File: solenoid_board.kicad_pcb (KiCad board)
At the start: 2 copper layers, 180 x 120 mm, 30 parts, among them J2 MCU_LEFT_LEGS, J3 MCU_RIGHT_LEGS

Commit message: Changed Geometry of PCB, removed edges, cleaned up displays. Next steps: routing.
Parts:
- 7Seg_1, 7Seg_2, 7Seg_3, 7Seg_4, 7Seg_5, 7Seg_6, 7Seg_7, 7Seg_8, 7Seg_9: moved to B.Cu
- moved R330 181.3 mm to (242.8, 50.7)
- moved R336 181.3 mm to (314.8, 50.7)
- moved R337 181.3 mm to (326.8, 50.7)
- moved R338 181.3 mm to (338.8, 50.7)
- moved R331 181.3 mm to (254.8, 50.7)
- moved R332 181.3 mm to (266.8, 50.7)
- moved R333 181.3 mm to (278.8, 50.7)
- moved R334 181.3 mm to (290.8, 50.7)
- moved R335 181.3 mm to (302.8, 50.7)
- moved 7Seg_6 59.5 mm to (161.8, 124.5), turned to 90 degrees
- moved 7Seg_5 55.2 mm to (146.8, 124.5), turned to 90 degrees
- moved 7Seg_4 55.0 mm to (131.8, 124.5), turned to 90 degrees
- moved 7Seg_3 45.6 mm to (116.8, 124.5), turned to 90 degrees
- moved 7Seg_7 43.5 mm to (88.1, 68.7), turned to 90 degrees
- moved 7Seg_1 42.8 mm to (86.8, 124.5), turned to 90 degrees
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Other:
- board outline removed

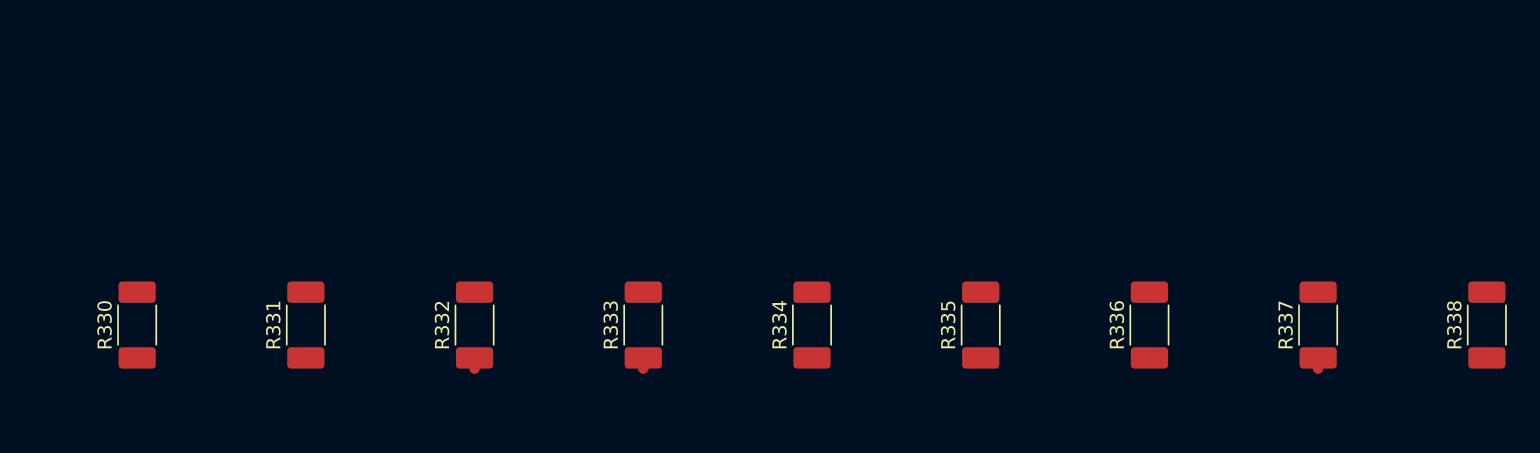
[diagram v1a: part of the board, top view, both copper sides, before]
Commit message: Changed resistor footprints, changed resistor supplier. Still need to route wires.
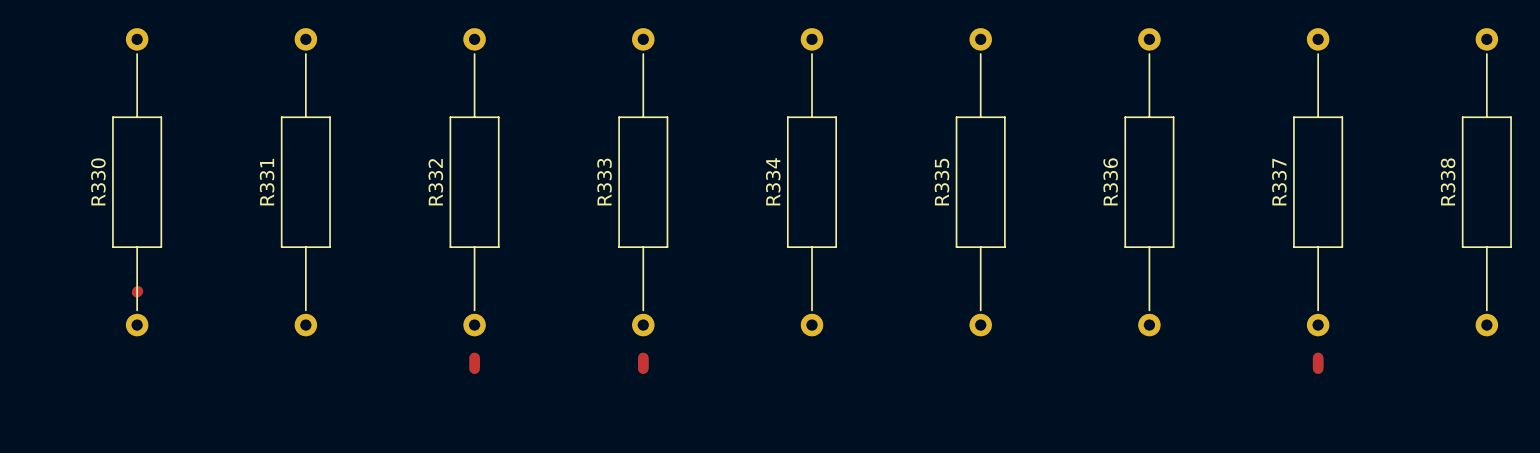
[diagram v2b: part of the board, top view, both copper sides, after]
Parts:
- R330, R331, R332, R333, R334, R335, R336, R337, R338: footprint Resistor_SMD:R_2010_5025Metric_Pad1.52x2.65mm_HandSolder -> Resistor_THT:R_Axial_DIN0309_L9.0mm_D3.2mm_P20.32mm_Horizontal

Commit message: Worked on Geometry of board. Needs to be finalized.
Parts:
- moved R336 232.4 mm to (83.0, 34.8), turned to 0 degrees
- moved R337 228.9 mm to (98.2, 38.9), turned to 0 degrees
- moved R338 225.7 mm to (113.2, 43.2), turned to 0 degrees
- moved R330 163.8 mm to (81.8, 80.9), turned to 0 degrees
- moved R331 161.7 mm to (96.8, 85.3), turned to 0 degrees
- moved R332 159.9 mm to (111.7, 89.7), turned to 0 degrees
- moved R333 158.1 mm to (126.6, 93.7), turned to 0 degrees
- moved R334 156.3 mm to (141.8, 97.7), turned to 0 degrees
- moved R335 154.8 mm to (156.8, 102.0), turned to 0 degrees
- moved C0.1nF0 21.6 mm to (215.8, 107.8)
- moved Prt_IC1 21.6 mm to (200.8, 104.7)
- moved J2 21.6 mm to (196.6, 60.3)
- moved CP0 21.6 mm to (220.6, 72.9)
- moved GND1 21.6 mm to (222.4, 113.0)
- moved J3 21.6 mm to (217.0, 70.4)
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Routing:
- net /First_Display: track 0.00 -> 43.6 mm
- net /Second_Display: track 0.00 -> 39.3 mm
- net /Third_Display: track 0.76 -> 34.9 mm
- net /Seventh_Display: track 0.00 -> 34.0 mm
- net /Fourth_Display: track 0.76 -> 30.9 mm
- net /Eigth_Display: track 0.76 -> 30.6 mm
- net /Fifth_Display: track 0.00 -> 26.8 mm
- net /Ninth_Display: track 0.00 -> 25.6 mm
- net /Sixth_Display: track 0.00 -> 22.6 mm
- net /DP: track 1.20 -> 0.00 mm

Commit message: Rearranged Component Geometry, switched out Transciever Resistor footprints, Routed Some wires.
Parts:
- R10, R11: footprint Resistor_SMD:R_2010_5025Metric_Pad1.52x2.65mm_HandSolder -> Resistor_THT:R_Axial_DIN0309_L9.0mm_D3.2mm_P20.32mm_Horizontal
- moved 7Seg_1 82.3 mm to (127.8, 53.2)
- moved 7Seg_2 82.3 mm to (142.8, 53.2)
- moved 7Seg_3 82.3 mm to (157.8, 53.2)
- moved R330 73.8 mm to (122.9, 19.6)
- moved R331 73.1 mm to (137.8, 24.8)
- moved R332 72.5 mm to (152.9, 30.0)
- moved R333 59.0 mm to (77.2, 61.5)
- moved R334 58.9 mm to (92.1, 66.0)
- moved R335 58.8 mm to (107.1, 70.4)
- moved R338 56.3 mm to (152.5, 83.6)
- moved 7Seg_7 56.2 mm to (127.6, 108.7)
- moved 7Seg_8 56.2 mm to (142.6, 108.7)
- moved 7Seg_9 56.2 mm to (157.6, 108.7)
- moved R336 56.2 mm to (122.5, 74.8)
- moved R337 56.2 mm to (137.7, 78.9)
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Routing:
- net /D10: track 0.00 -> 148.2 mm
- net /D13: track 0.00 -> 136.3 mm
- net /D9: track 0.00 -> 131.0 mm
- net /D12: track 0.00 -> 118.1 mm
- net /D6: track 0.00 -> 113.5 mm
- net /D11: track 0.00 -> 100.6 mm
- net /A3: track 0.00 -> 96.1 mm
- net /D5: track 0.00 -> 95.3 mm
- net /SCL: track 0.00 -> 77.2 mm
- net /SDA: track 0.00 -> 59.4 mm
- net /Fourth_Display: track 30.9 -> 47.1 mm
- net /Fifth_Display: track 26.8 -> 42.7 mm
- net /Sixth_Display: track 22.6 -> 38.3 mm
- net /RJ45_5: track 73.8 -> 61.8 mm, vias 0 -> 1
- net /Third_Display: track 34.9 -> 23.3 mm
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
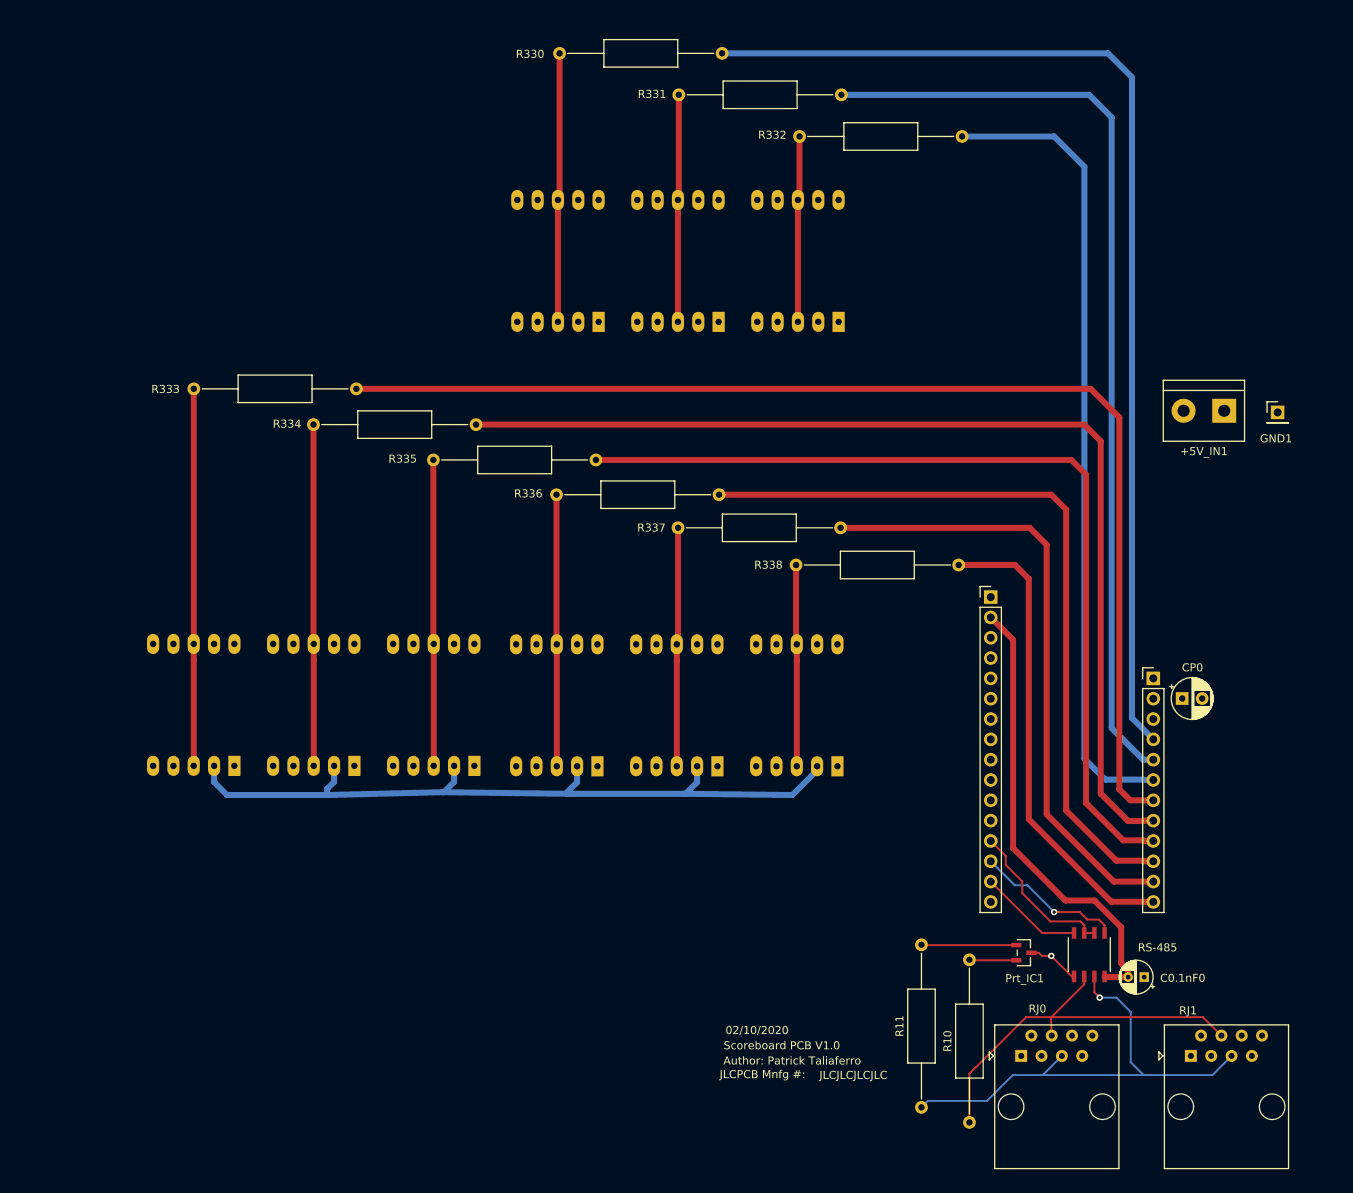
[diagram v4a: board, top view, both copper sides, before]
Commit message: Finished Routing and generated new .gbr files. I am unsatisfied with the size of the board, and the geometry may need to be moved around to allow ball count to be displayed underneath the score.
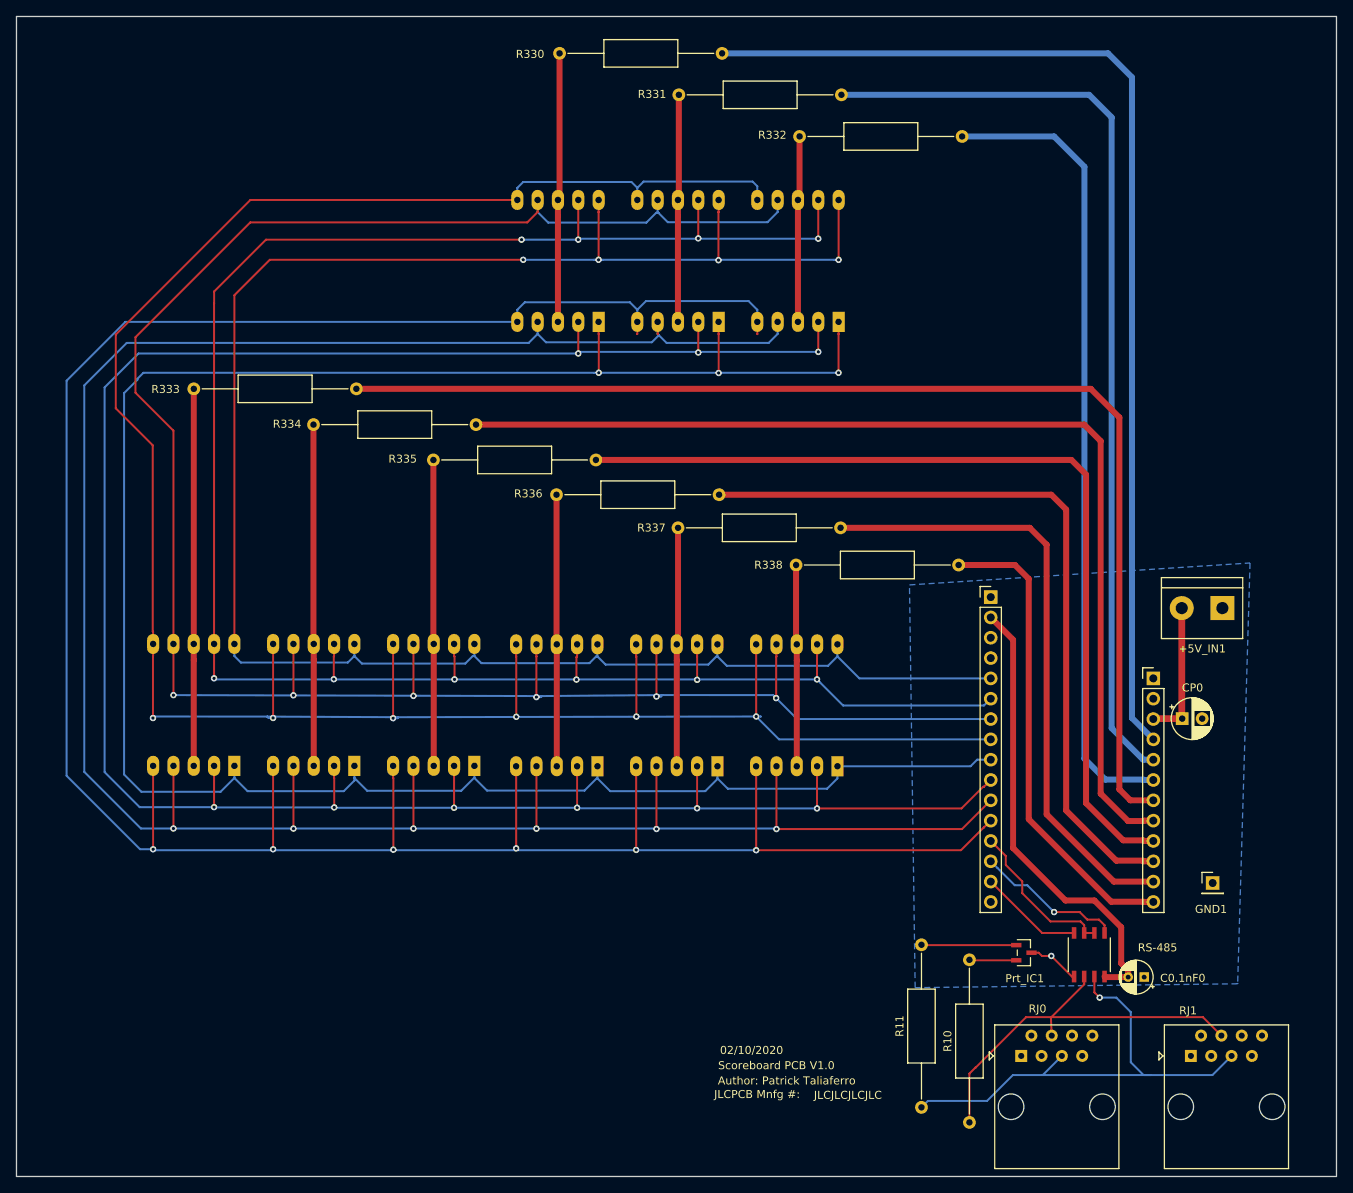
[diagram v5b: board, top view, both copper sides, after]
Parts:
- moved GND1 59.4 mm to (204.5, 123.3)
- moved +5V_IN1 24.7 mm to (205.7, 89.0)
- moved CP0 2.51 mm to (200.7, 102.8)
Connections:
- 7Seg_1 pad 10: /G -> /A0
- 7Seg_1 pad 2: /A3 -> /A5
- 7Seg_1 pad 4: /A2 -> /C
- 7Seg_1 pad 6: /A1 -> /A3
- 7Seg_1 pad 9: /A5 -> /A1
- 7Seg_2 pad 10: /G -> /A0
- 7Seg_2 pad 2: /A3 -> /A5
- 7Seg_2 pad 4: /A2 -> /C
- 7Seg_2 pad 6: /A1 -> /A3
- 7Seg_2 pad 9: /A5 -> /A1
- 7Seg_3 pad 10: /G -> /A0
- 7Seg_3 pad 2: /A3 -> /A5
- 7Seg_3 pad 4: /A2 -> /C
- 7Seg_3 pad 6: /A1 -> /A3
- 7Seg_3 pad 9: /A5 -> /A1
- 7Seg_4 pad 10: /G -> /A0
- 7Seg_4 pad 2: /A3 -> /A5
- 7Seg_4 pad 4: /A2 -> /C
- 7Seg_4 pad 6: /A1 -> /A3
- 7Seg_4 pad 9: /A5 -> /A1
- 7Seg_5 pad 10: /G -> /A0
- 7Seg_5 pad 2: /A3 -> /A5
- 7Seg_5 pad 4: /A2 -> /C
- 7Seg_5 pad 6: /A1 -> /A3
- 7Seg_5 pad 9: /A5 -> /A1
- 7Seg_6 pad 10: /G -> /A0
- 7Seg_6 pad 2: /A3 -> /A5
- 7Seg_6 pad 4: /A2 -> /C
- 7Seg_6 pad 6: /A1 -> /A3
- 7Seg_6 pad 9: /A5 -> /A1
- 7Seg_7 pad 10: /G -> /A0
- 7Seg_7 pad 2: /A3 -> /A5
- 7Seg_7 pad 4: /A2 -> /C
- 7Seg_7 pad 6: /A1 -> /A3
- 7Seg_7 pad 9: /A5 -> /A1
- 7Seg_8 pad 10: /G -> /A0
- 7Seg_8 pad 2: /A3 -> /A5
- 7Seg_8 pad 4: /A2 -> /C
- 7Seg_8 pad 6: /A1 -> /A3
- 7Seg_8 pad 9: /A5 -> /A1
- 7Seg_9 pad 10: /G -> /A0
- 7Seg_9 pad 2: /A3 -> /A5
- 7Seg_9 pad 4: /A2 -> /C
- 7Seg_9 pad 6: /A1 -> /A3
- 7Seg_9 pad 9: /A5 -> /A1
- J2 pad 11: /G -> /C
- J2 pad 5: /A -> /A0
- J2 pad 7: /A2 -> /A
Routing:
- net /DP: track 0.00 -> 331.7 mm, vias 0 -> 6
- net /C: track 0.00 -> 310.4 mm, vias 0 -> 6
- net /A5: track 0.00 -> 296.1 mm, vias 0 -> 9
- net /A4: track 0.00 -> 283.2 mm, vias 0 -> 3
- net /A: track 0.00 -> 279.7 mm, vias 0 -> 6
- net /A1: track 0.00 -> 262.2 mm, vias 0 -> 10
- net /A0: track 0.00 -> 252.2 mm, vias 0 -> 4
- net /A3: track 96.1 -> 296.7 mm, vias 0 -> 6
- net +5V: track 0.00 -> 17.5 mm
- added copper zone on B.Cu, net GND
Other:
- board outline added: 165 x 145 mm

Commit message: Added Mounting Holes
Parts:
- added REF**: MountingHole_2.7mm_M2.5, MountingHole:MountingHole_2.7mm_M2.5, F.Cu at (60.0, 155.0)
- added REF**: MountingHole_2.7mm_M2.5, MountingHole:MountingHole_2.7mm_M2.5, F.Cu at (60.0, 20.0)
- added REF**: MountingHole_2.7mm_M2.5, MountingHole:MountingHole_2.7mm_M2.5, F.Cu at (220.0, 155.0)
- added REF**: MountingHole_2.7mm_M2.5, MountingHole:MountingHole_2.7mm_M2.5, F.Cu at (220.0, 20.0)
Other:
- board size 165 x 145 mm -> 170 x 145 mm

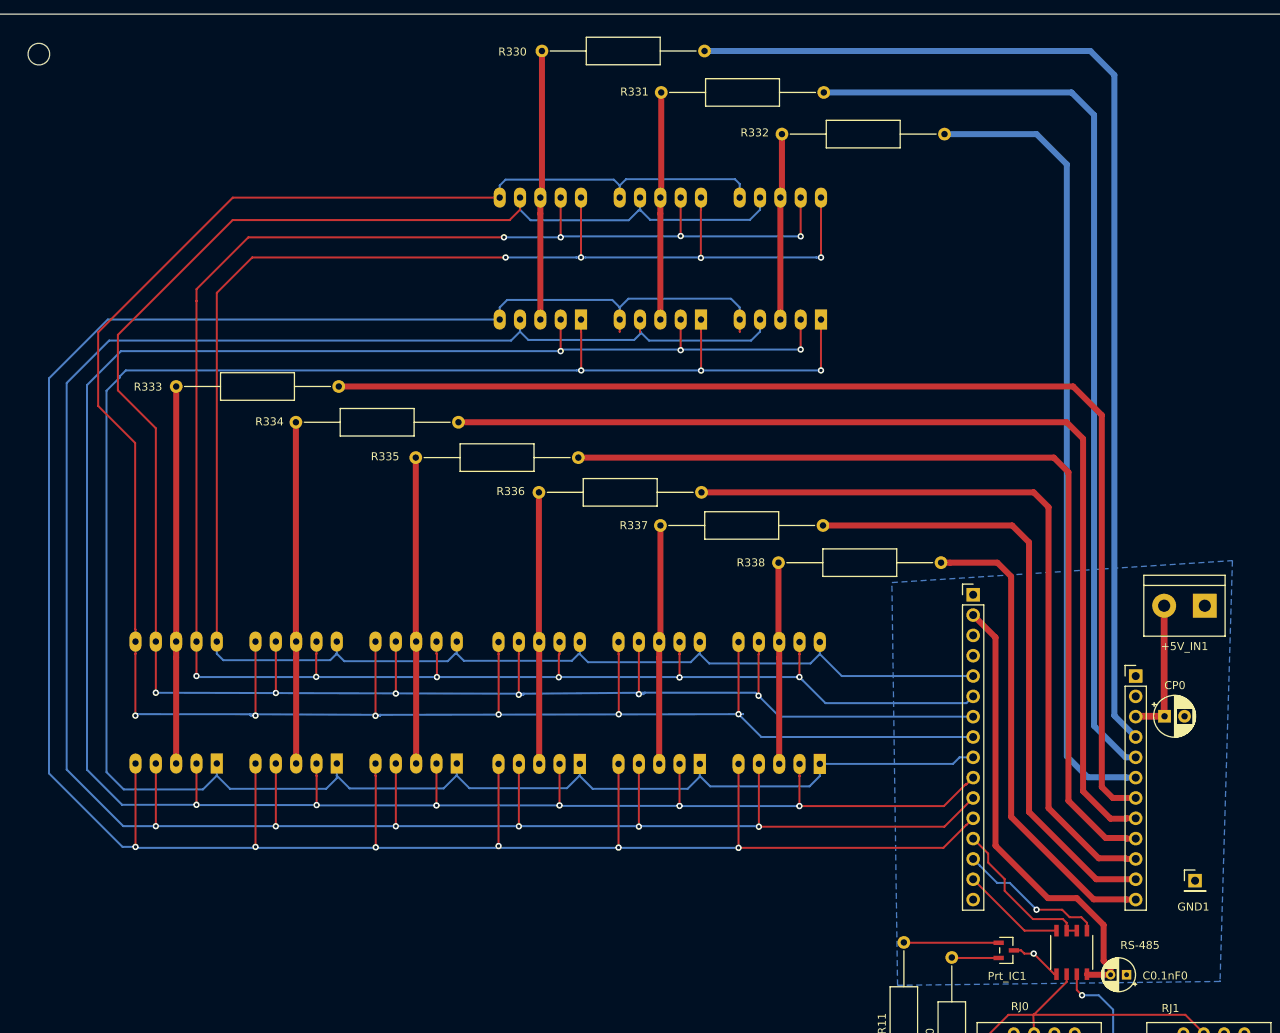
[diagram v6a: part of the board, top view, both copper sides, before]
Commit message: Deleted all the wire routes related to the scoreboard.
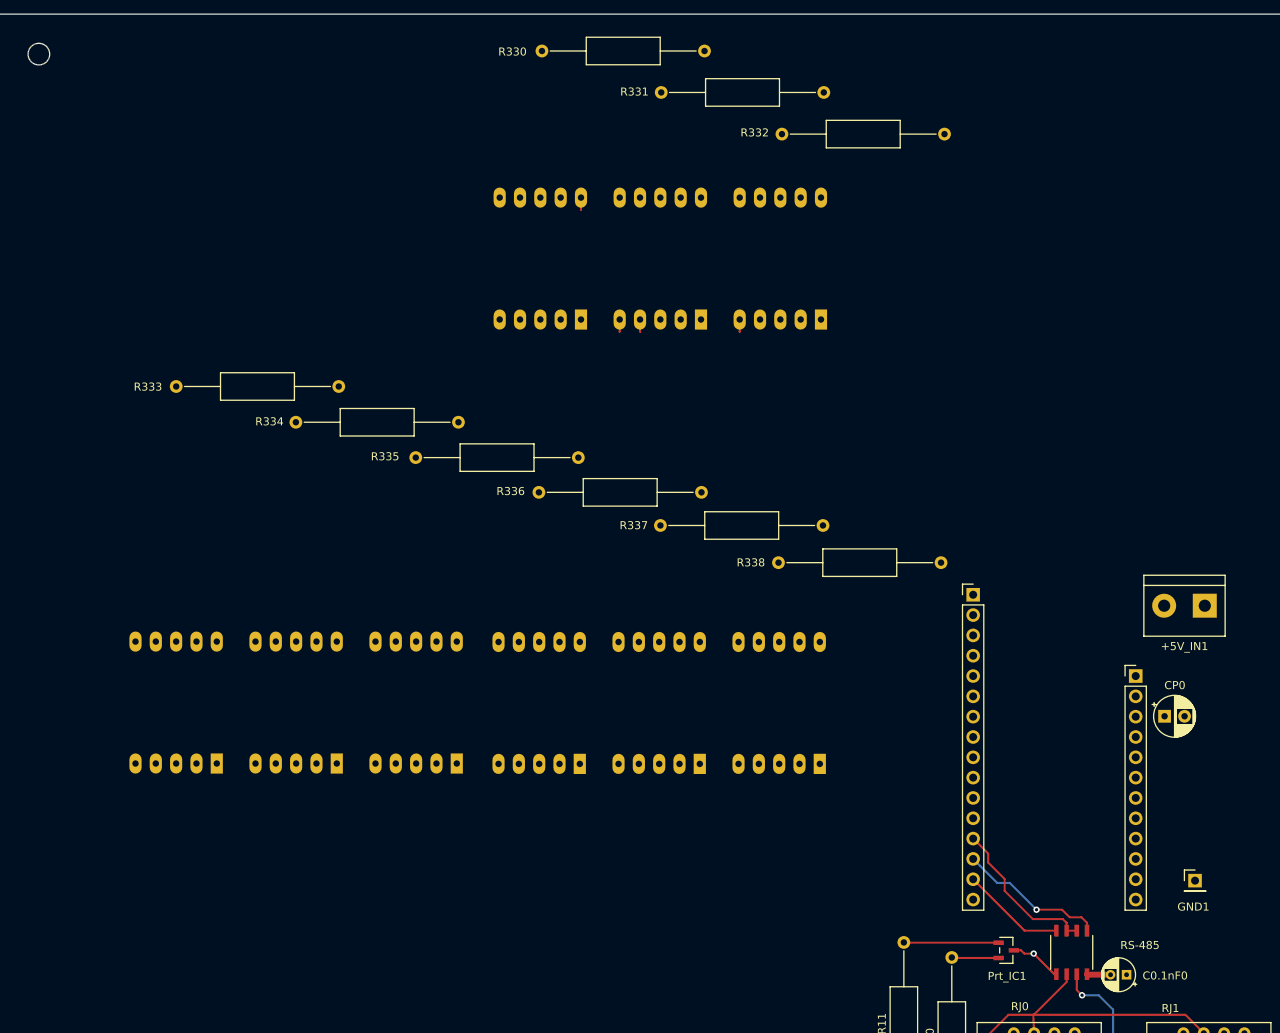
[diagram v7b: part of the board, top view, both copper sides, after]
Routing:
- net /DP: track 331.7 -> 3.08 mm, vias 6 -> 0
- net /C: track 310.4 -> 1.56 mm, vias 6 -> 0
- net /A3: track 296.7 -> 0.00 mm, vias 6 -> 0
- net /A5: track 296.1 -> 0.00 mm, vias 9 -> 0
- net /A4: track 283.2 -> 0.00 mm, vias 3 -> 0
- net /A: track 279.7 -> 0.00 mm, vias 6 -> 0
- net /A1: track 262.2 -> 0.00 mm, vias 10 -> 0
- net /A0: track 252.2 -> 1.52 mm, vias 4 -> 0
- net /D10: track 148.2 -> 0.00 mm
- net /D13: track 136.3 -> 0.00 mm
- net /D9: track 131.0 -> 0.00 mm
- net /D12: track 118.1 -> 0.00 mm
- net /D6: track 113.5 -> 0.00 mm
- net /D11: track 100.6 -> 0.00 mm
- net /D5: track 95.3 -> 0.00 mm
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- removed copper zone on B.Cu, net GND
